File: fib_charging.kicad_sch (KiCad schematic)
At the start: 49 parts, among them J301 Conn_01x02, J302 Conn_01x02, J303 Conn_01x02, Q301 CSD17581Q3A, Q302 CSD17581Q3A, Q303 CSD17581Q3A, Q304 CSD17581Q3A, U301 BQ25798RQMR

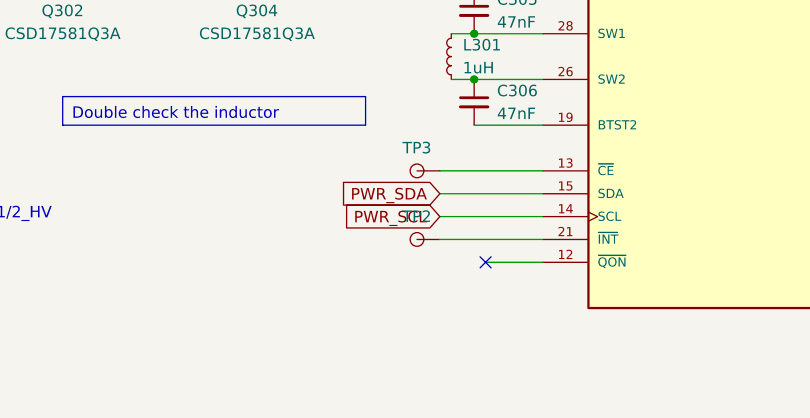
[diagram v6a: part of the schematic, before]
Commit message: finished routing, sanity check and prep fabrication files next
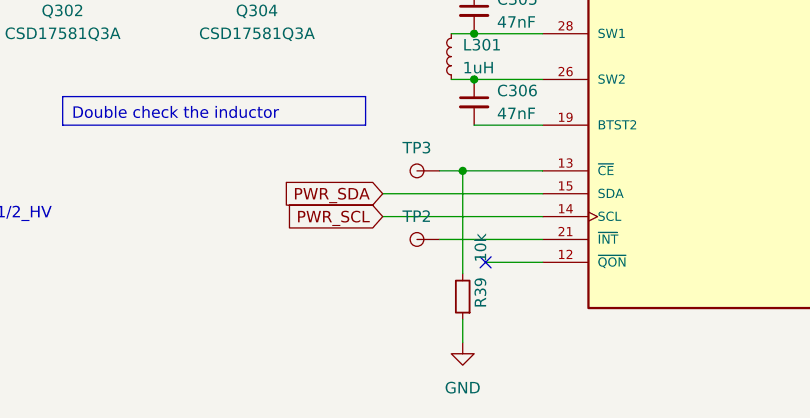
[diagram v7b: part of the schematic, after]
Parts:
- added R39: 10K, Resistor_SMD:R_0402_1005Metric, symbol Fibel2:R_Small_Rota
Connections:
- net GND: now also R39.1
- net at TP3.1, U301.13 (~{CE}): now also R39.2
